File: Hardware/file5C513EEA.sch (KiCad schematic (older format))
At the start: 84 parts, among them J10 IN_2, J11 IN_3, J12 PWM_CV, J13 EXT_CON, J4 OUT2_CON, J5 CUTOFF_CV, J6 SHAPE_CV, J7 SET_CV, J8 OUT1_CON, J9 IN_1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

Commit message: Updated ADSR sliders
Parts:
- removed RV5: ATTACK, Potentiometer_THT:Potentiometer_Bourns_PTA2043_Single_Slide, symbol Device:R_POT_US
- removed RV6: SUSTAIN, Potentiometer_THT:Potentiometer_Bourns_PTA2043_Single_Slide, symbol Device:R_POT_US
- removed RV7: DECAY, Potentiometer_THT:Potentiometer_Bourns_PTA2043_Single_Slide, symbol Device:R_POT_US
- removed RV8: RELEASE, Potentiometer_THT:Potentiometer_Bourns_PTA2043_Single_Slide, symbol Device:R_POT_US
- added RV5: ATTACK, Potentiometer_THT:Potentiometer_Bourns_PTL20_Single_Slide, symbol SID_Parts:BOURNS_PTL
- added RV6: DECAY, Potentiometer_THT:Potentiometer_Bourns_PTL20_Single_Slide, symbol SID_Parts:BOURNS_PTL
- added RV7: SUSTAIN, Potentiometer_THT:Potentiometer_Bourns_PTL20_Single_Slide, symbol SID_Parts:BOURNS_PTL
- added RV8: RELEASE, Potentiometer_THT:Potentiometer_Bourns_PTL20_Single_Slide, symbol SID_Parts:BOURNS_PTL
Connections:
- net 3.3A_IO: now also RV5.1, RV6.1, RV7.1, RV8.1
- net ATTACK_IO: now also RV5.2
- net DECAY_IO: now also RV6.2
- net GND: now also RV5.3, RV6.3, RV7.3, RV8.3
- net RELEASE_IO: now also RV8.2
- net SUSTAIN_IO: now also RV7.2
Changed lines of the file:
@@
 Wire Wire Line
 	1300 4100 1250 4100
-$Comp
-L Device:R_POT_US RV?
-U 1 1 5C5721BD
-P 2200 950
-AR Path="/5BFD63E3/5C5721BD" Ref="RV?"  Part="1"
-AR Path="/5BFD63E3/5C513EEB/5C5721BD" Ref="RV5"  Part="1"
-F 0 "RV5" H 2132 996 50  0000 R CNN
-F 1 "ATTACK" H 2132 905 50  0000 R CNN
-F 2 "Potentiometer_THT:Potentiometer_Bourns_PTA2043_Single_Slide" H 2200 950 50  0001 C CNN
-F 3 "~" H 2200 950 50  0001 C CNN
-	1    2200 950
-	1    0    0    -1
-$EndComp
 Wire Wire Line
 	2200 750  2200 800
@@
 	2450 950  2400 950
 $Comp
-L Device:R_POT_US RV?
-U 1 1 5C5721D4
-P 2300 2050
-AR Path="/5BFD63E3/5C5721D4" Ref="RV?"  Part="1"
-AR Path="/5BFD63E3/5C513EEB/5C5721D4" Ref="RV7"  Part="1"
-F 0 "RV7" H 2232 2096 50  0000 R CNN
-F 1 "DECAY" H 2232 2005 50  0000 R CNN
-F 2 "Potentiometer_THT:Potentiometer_Bourns_PTA2043_Single_Slide" H 2300 2050 50  0001 C CNN
-F 3 "~" H 2300 2050 50  0001 C CNN
-	1    2300 2050
-	1    0    0    -1
-$EndComp
-$Comp
 L power:GND #PWR?
 U 1 1 5C5721E2
@@
 Wire Wire Line
 	2550 2050 2500 2050
-$Comp
-L Device:R_POT_US RV?
-U 1 1 5C5721EB
-P 2200 3150
-AR Path="/5BFD63E3/5C5721EB" Ref="RV?"  Part="1"
-AR Path="/5BFD63E3/5C513EEB/5C5721EB" Ref="RV6"  Part="1"
-F 0 "RV6" H 2132 3196 50  0000 R CNN
-F 1 "SUSTAIN" H 2132 3105 50  0000 R CNN
-F 2 "Potentiometer_THT:Potentiometer_Bourns_PTA2043_Single_Slide" H 2200 3150 50  0001 C CNN
-F 3 "~" H 2200 3150 50  0001 C CNN
-	1    2200 3150
-	1    0    0    -1
-$EndComp
 Wire Wire Line
 	2200 2950 2200 3000
@@
 Wire Wire Line
 	2450 3150 2400 3150
-$Comp
-L Device:R_POT_US RV?
-U 1 1 5C572202
-P 3350 950
-AR Path="/5BFD63E3/5C572202" Ref="RV?"  Part="1"
-AR Path="/5BFD63E3/5C513EEB/5C572202" Ref="RV8"  Part="1"
-F 0 "RV8" H 3282 996 50  0000 R CNN
-F 1 "RELEASE" H 3282 905 50  0000 R CNN
-F 2 "Potentiometer_THT:Potentiometer_Bourns_PTA2043_Single_Slide" H 3350 950 50  0001 C CNN
-F 3 "~" H 3350 950 50  0001 C CNN
-	1    3350 950
-	1    0    0    -1
-$EndComp
 Wire Wire Line
 	3350 750  3350 800
@@
 $Comp
 L Device:C C?
-U 1 1 5C57223C
-P 2400 3350
-AR Path="/5BFD63E3/5C57223C" Ref="C?"  Part="1"
-AR Path="/5BFD63E3/5C513EEB/5C57223C" Ref="C16"  Part="1"
-F 0 "C16" H 2515 3396 50  0000 L CNN
-F 1 "100 nF" H 2515 3305 50  0000 L CNN
-F 2 "Capacitor_SMD:C_0603_1608Metric" H 2438 3200 50  0001 C CNN
-F 3 "~" H 2400 3350 50  0001 C CNN
-	1    2400 3350
-	1    0    0    -1
-$EndComp
-$Comp
-L Device:C C?
 U 1 1 5C572243
 P 3550 1150
@@
 Wire Wire Line
 	2400 3200 2400 3150
-Connection ~ 2400 3150
-Wire Wire Line
-	2400 3150 2350 3150
 Wire Wire Line
 	3550 1000 3550 950
@@
 F 3 "http://ww1.microchip.com/downloads/en/DeviceDoc/21733j.pdf" H 5150 7000 50  0001 C CNN
 	3    5150 7000
-	1    0    0    -1
-$EndComp
-$Comp
-L Device:R_POT_US RV?
-U 1 1 5BF0EB16
-P 3350 2100
-AR Path="/5BFD63E3/5BF0EB16" Ref="RV?"  Part="1"
-AR Path="/5BFD63E3/5C513EEB/5BF0EB16" Ref="RV10"  Part="1"
-F 0 "RV10" H 3282 2146 50  0000 R CNN
-F 1 "SET_ATTEN" H 3282 2055 50  0000 R CNN
-F 2 "Potentiometer_THT:Potentiometer_Bourns_PTV09A-1_Single_Vertical" H 3350 2100 50  0001 C CNN
-F 3 "~" H 3350 2100 50  0001 C CNN
-	1    3350 2100
 	1    0    0    -1
 $EndComp
@@
 Text GLabel 9400 1050 0    50   Input ~ 0
 -10V_REF_IO
+$Comp
+L SID_Parts:BOURNS_PTL RV5
+U 1 1 5BEA495C
+P 2200 700
+F 0 "RV5" H 2112 496 50  0000 R CNN
+F 1 "ATTACK" H 2112 405 50  0000 R CNN
+F 2 "Potentiometer_THT:Potentiometer_Bourns_PTL20_Single_Slide" H 2200 700 50  0001 C CNN
+F 3 "" H 2200 700 50  0001 C CNN
+	1    2200 700
+	1    0    0    -1
+$EndComp
+Connection ~ 2400 3150
+Wire Wire Line
+	2400 3150 2350 3150
+$Comp
+L Device:C C?
+U 1 1 5C57223C
+P 2400 3350
+AR Path="/5BFD63E3/5C57223C" Ref="C?"  Part="1"
+AR Path="/5BFD63E3/5C513EEB/5C57223C" Ref="C16"  Part="1"
+F 0 "C16" H 2515 3396 50  0000 L CNN
+F 1 "100 nF" H 2515 3305 50  0000 L CNN
+F 2 "Capacitor_SMD:C_0603_1608Metric" H 2438 3200 50  0001 C CNN
+F 3 "~" H 2400 3350 50  0001 C CNN
+	1    2400 3350
+	1    0    0    -1
+$EndComp
+$Comp
+L Device:R_POT_US RV?
+U 1 1 5BF0EB16
+P 3350 2100
+AR Path="/5BFD63E3/5BF0EB16" Ref="RV?"  Part="1"
+AR Path="/5BFD63E3/5C513EEB/5BF0EB16" Ref="RV10"  Part="1"
+F 0 "RV10" H 3282 2146 50  0000 R CNN
+F 1 "SET_ATTEN" H 3282 2055 50  0000 R CNN
+F 2 "Potentiometer_THT:Potentiometer_Bourns_PTV09A-1_Single_Vertical" H 3350 2100 50  0001 C CNN
+F 3 "~" H 3350 2100 50  0001 C CNN
+	1    3350 2100
+	1    0    0    -1
+$EndComp
+$Comp
+L SID_Parts:BOURNS_PTL RV8
+U 1 1 5C03E468
+P 3350 700
+F 0 "RV8" H 3262 496 50  0000 R CNN
+F 1 "RELEASE" H 3262 405 50  0000 R CNN
+F 2 "Potentiometer_THT:Potentiometer_Bourns_PTL20_Single_Slide" H 3350 700 50  0001 C CNN
+F 3 "" H 3350 700 50  0001 C CNN
+	1    3350 700
+	1    0    0    -1
+$EndComp
+$Comp
+L SID_Parts:BOURNS_PTL RV6
+U 1 1 5C057FF7
+P 2300 1800
+F 0 "RV6" H 2212 1596 50  0000 R CNN
+F 1 "DECAY" H 2212 1505 50  0000 R CNN
+F 2 "Potentiometer_THT:Potentiometer_Bourns_PTL20_Single_Slide" H 2300 1800 50  0001 C CNN
+F 3 "" H 2300 1800 50  0001 C CNN
+	1    2300 1800
+	1    0    0    -1
+$EndComp
+$Comp
+L SID_Parts:BOURNS_PTL RV7
+U 1 1 5C071B88
+P 2200 2900
+F 0 "RV7" H 2112 2696 50  0000 R CNN
+F 1 "SUSTAIN" H 2112 2605 50  0000 R CNN
+F 2 "Potentiometer_THT:Potentiometer_Bourns_PTL20_Single_Slide" H 2200 2900 50  0001 C CNN
+F 3 "" H 2200 2900 50  0001 C CNN
+	1    2200 2900
+	1    0    0    -1
+$EndComp
 $EndSCHEMATC

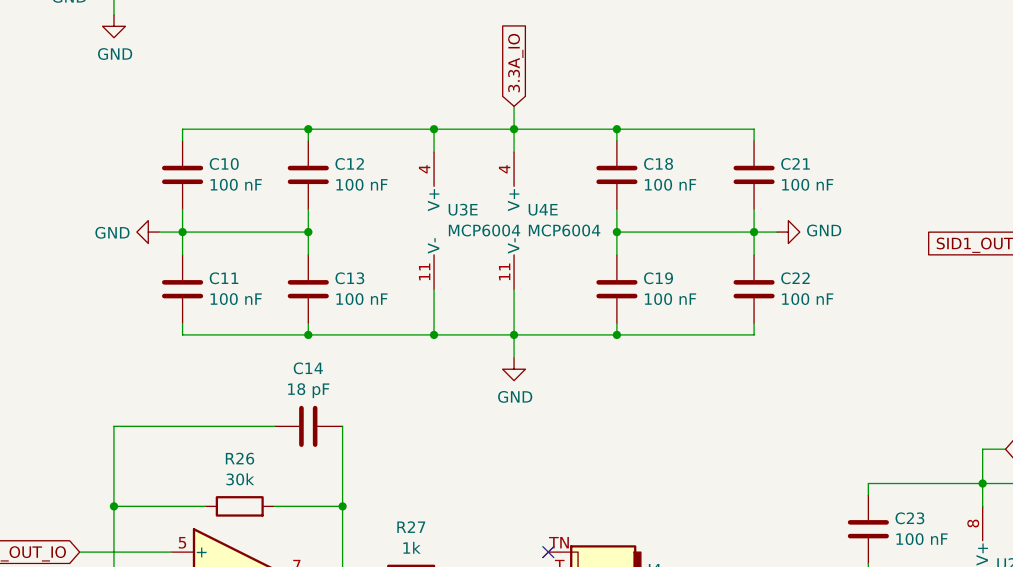
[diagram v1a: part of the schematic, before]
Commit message: More wiring, removed pointless capacitors
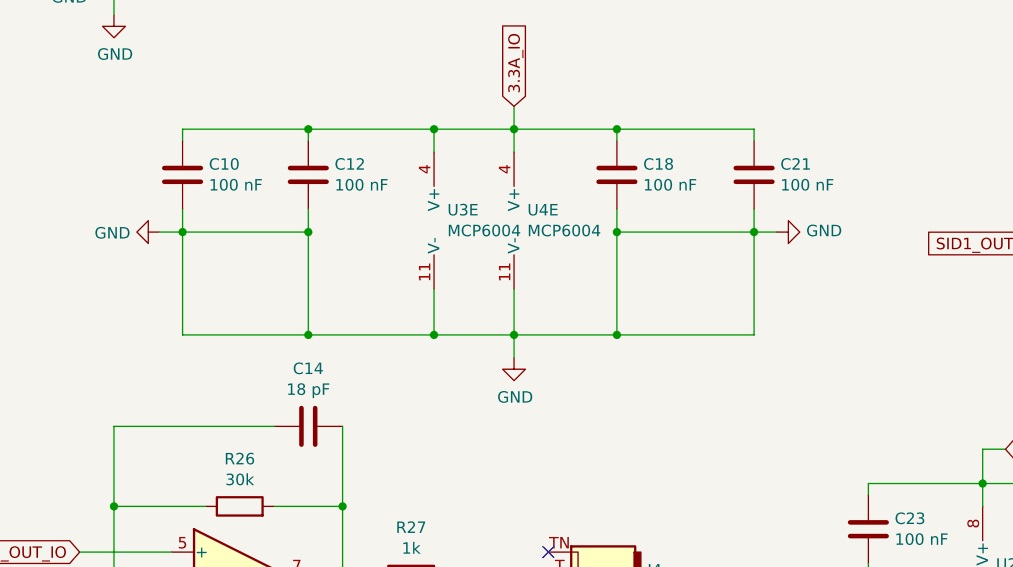
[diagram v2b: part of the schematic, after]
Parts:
- removed C11, C13, C19, C22: 100 nF, Capacitor_SMD:C_0603_1608Metric, symbol Device:C
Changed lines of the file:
@@
 	1    0    0    -1
 $EndComp
-$Comp
-L Device:C C?
-U 1 1 5C593892
-P 1550 5750
-AR Path="/5BFD63E3/5C593892" Ref="C?"  Part="1"
-AR Path="/5BFD63E3/5C513EEB/5C593892" Ref="C11"  Part="1"
-F 0 "C11" H 1665 5796 50  0000 L CNN
-F 1 "100 nF" H 1665 5705 50  0000 L CNN
-F 2 "Capacitor_SMD:C_0603_1608Metric" H 1588 5600 50  0001 C CNN
-F 3 "~" H 1550 5750 50  0001 C CNN
-	1    1550 5750
-	1    0    0    -1
-$EndComp
-$Comp
-L Device:C C?
-U 1 1 5C593899
-P 3450 5750
-AR Path="/5BFD63E3/5C593899" Ref="C?"  Part="1"
-AR Path="/5BFD63E3/5C513EEB/5C593899" Ref="C19"  Part="1"
-F 0 "C19" H 3565 5796 50  0000 L CNN
-F 1 "100 nF" H 3565 5705 50  0000 L CNN
-F 2 "Capacitor_SMD:C_0603_1608Metric" H 3488 5600 50  0001 C CNN
-F 3 "~" H 3450 5750 50  0001 C CNN
-	1    3450 5750
-	1    0    0    -1
-$EndComp
-Wire Wire Line
-	1550 5900 1550 5950
 Connection ~ 3000 5950
-Wire Wire Line
-	3450 5950 3450 5900
 Wire Wire Line
 	1550 5100 1550 5050
@@
 Wire Wire Line
 	1550 5500 1550 5400
-Wire Wire Line
-	1550 5600 1550 5500
 Connection ~ 1550 5500
 $Comp
@@
 	1    0    0    -1
 $EndComp
-$Comp
-L Device:C C?
-U 1 1 5C16FA07
-P 4050 5750
-AR Path="/5BFD63E3/5C16FA07" Ref="C?"  Part="1"
-AR Path="/5BFD63E3/5C513EEB/5C16FA07" Ref="C22"  Part="1"
-F 0 "C22" H 4165 5796 50  0000 L CNN
-F 1 "100 nF" H 4165 5705 50  0000 L CNN
-F 2 "Capacitor_SMD:C_0603_1608Metric" H 4088 5600 50  0001 C CNN
-F 3 "~" H 4050 5750 50  0001 C CNN
-	1    4050 5750
-	1    0    0    -1
-$EndComp
 Wire Wire Line
 	3450 5050 4050 5050
@@
 Wire Wire Line
 	3450 5950 4050 5950
-Wire Wire Line
-	4050 5950 4050 5900
 Connection ~ 3450 5950
 Wire Wire Line
@@
 	4150 5500 4050 5500
 Connection ~ 4050 5500
-Wire Wire Line
-	4050 5500 4050 5600
 $Comp
 L Device:C C?
@@
 	1    0    0    -1
 $EndComp
-$Comp
-L Device:C C?
-U 1 1 5C1D88B3
-P 2100 5750
-AR Path="/5BFD63E3/5C1D88B3" Ref="C?"  Part="1"
-AR Path="/5BFD63E3/5C513EEB/5C1D88B3" Ref="C13"  Part="1"
-F 0 "C13" H 2215 5796 50  0000 L CNN
-F 1 "100 nF" H 2215 5705 50  0000 L CNN
-F 2 "Capacitor_SMD:C_0603_1608Metric" H 2138 5600 50  0001 C CNN
-F 3 "~" H 2100 5750 50  0001 C CNN
-	1    2100 5750
-	1    0    0    -1
-$EndComp
 Wire Wire Line
 	1550 5050 2100 5050
@@
 Wire Wire Line
 	1550 5500 2100 5500
-Connection ~ 2100 5500
-Wire Wire Line
-	2100 5500 2100 5600
-Wire Wire Line
-	2100 5950 2100 5900
 Wire Wire Line
 	1550 5950 2100 5950
@@
 	2650 5750 2650 5950
 Connection ~ 3450 5500
-Wire Wire Line
-	3450 5500 3450 5600
 $Comp
 L Device:D_Zener D?
@@
 	1    0    0    -1
 $EndComp
+Wire Wire Line
+	1550 5500 1550 5950
+Wire Wire Line
+	2100 5500 2100 5950
+Connection ~ 2100 5500
+Wire Wire Line
+	3450 5500 3450 5950
+Wire Wire Line
+	4050 5500 4050 5950
 $EndSCHEMATC

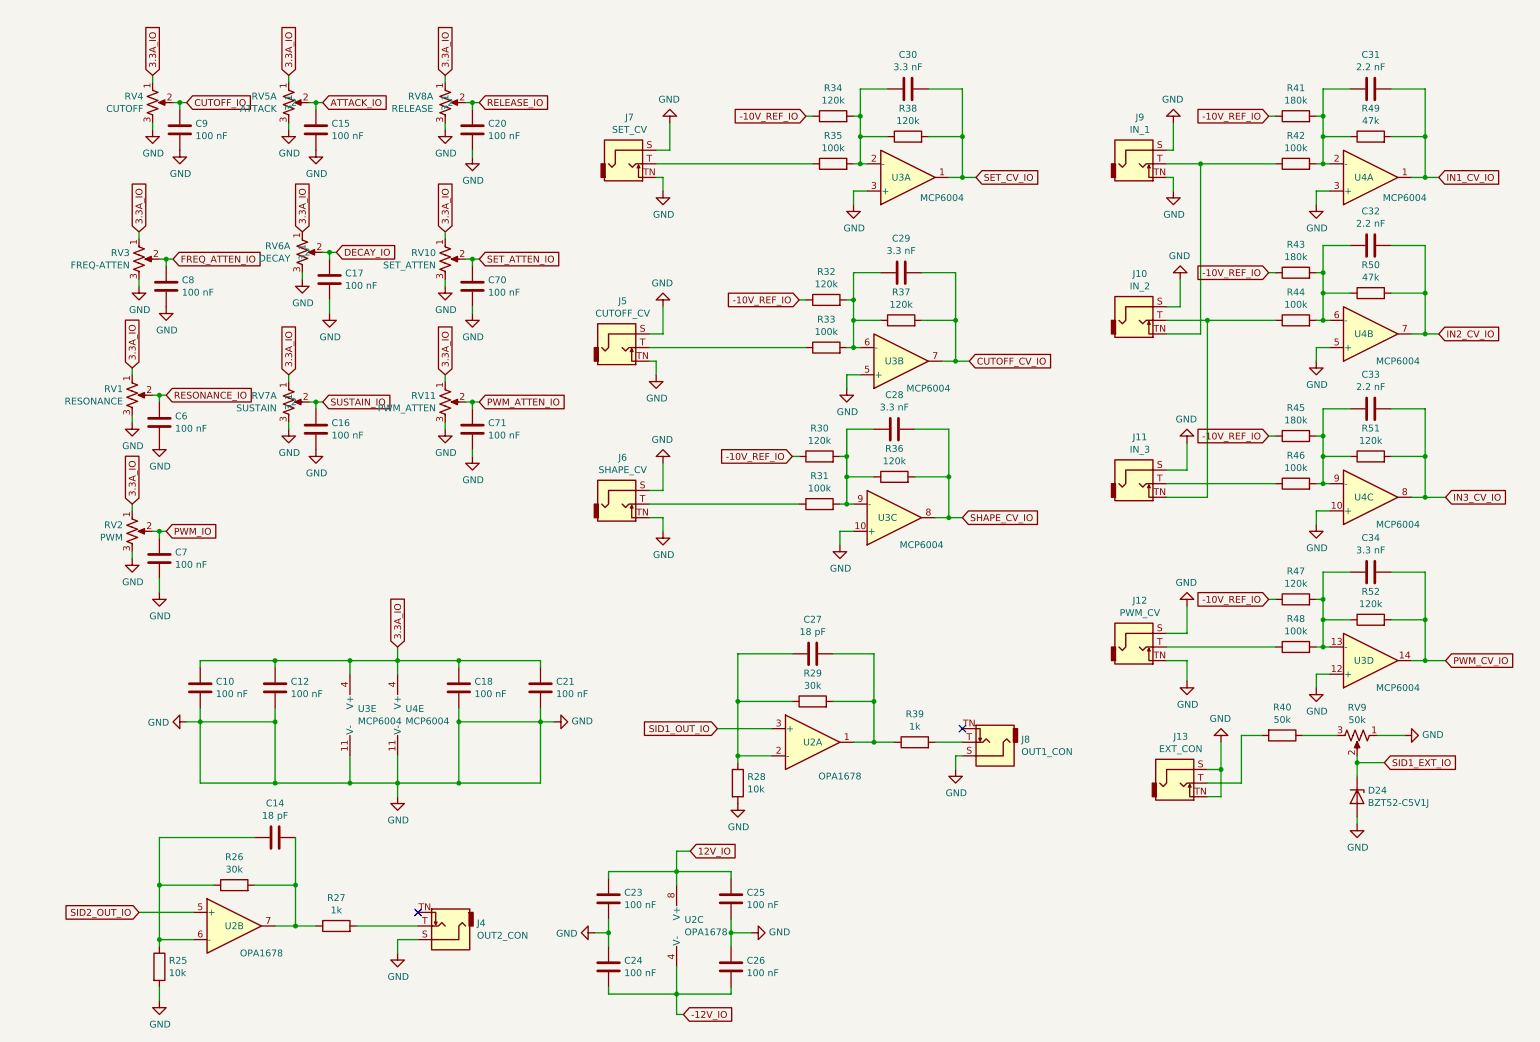
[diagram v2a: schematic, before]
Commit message: Updated to single four layer board
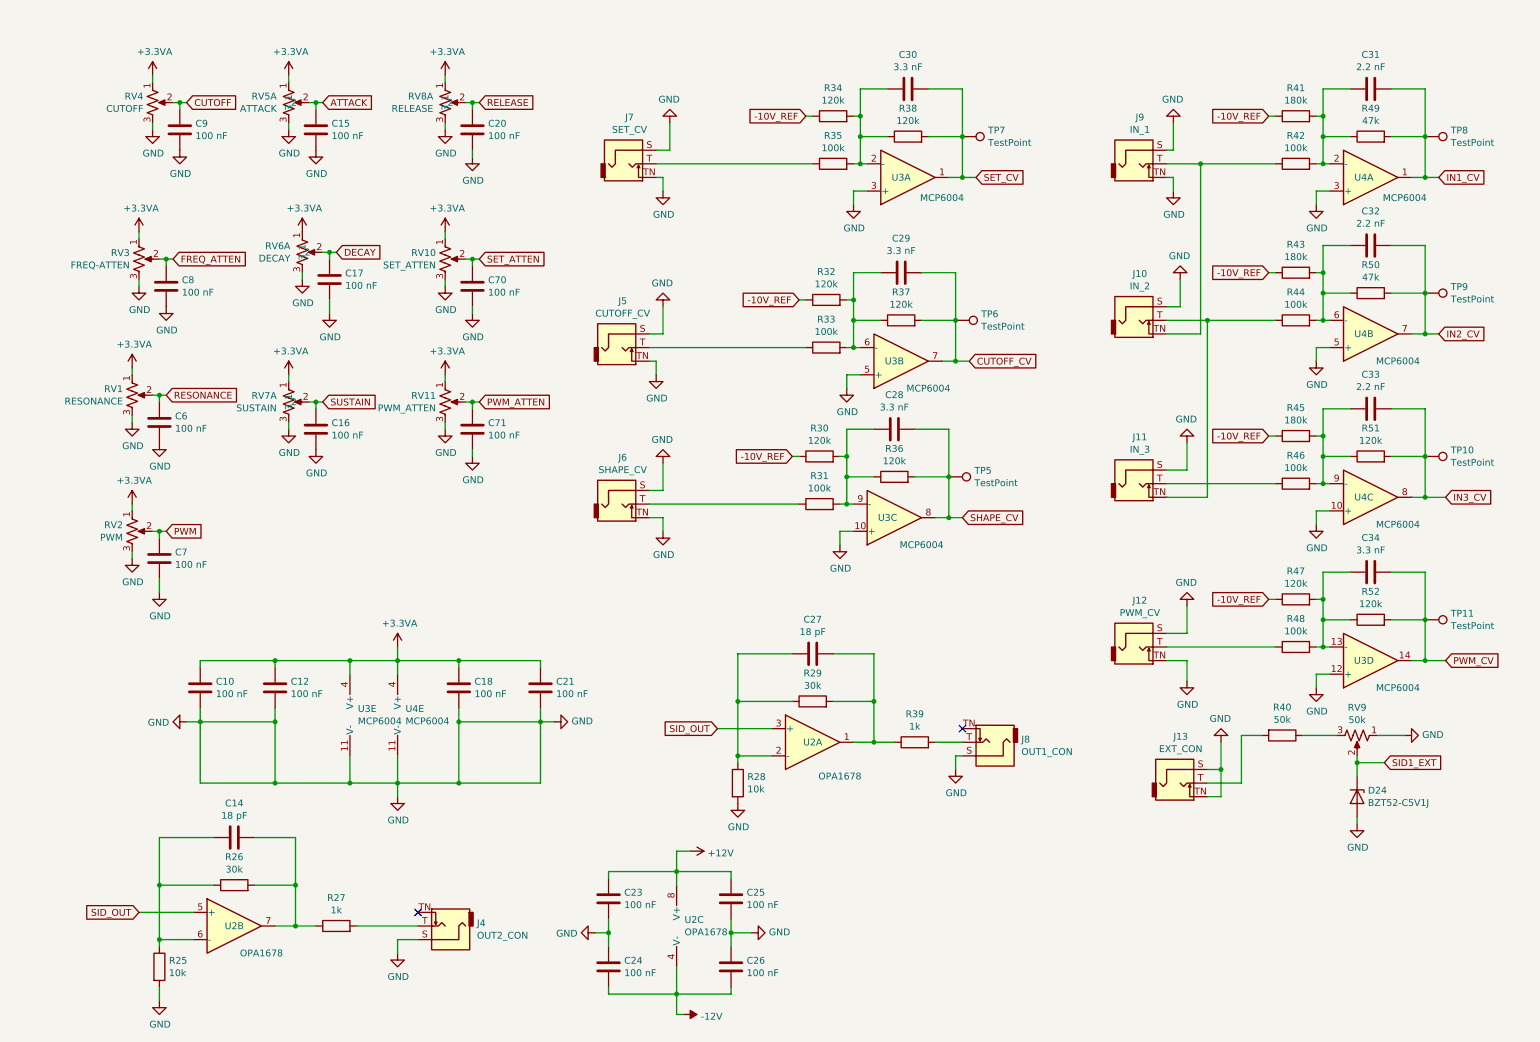
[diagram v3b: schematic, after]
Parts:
- added TP10, TP11, TP5, TP6, TP7, TP8, TP9: TestPoint, TestPoint:TestPoint_Pad_D1.0mm, symbol Connector:TestPoint
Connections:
- net SID2_OUT_IO is gone; now on net SID_OUT: U2.5 (+)
- net -10V_REF_IO renamed -10V_REF
- net -12V_IO renamed -12V
- net 12V_IO renamed +12V
- net 3.3A_IO renamed +3.3VA
- net ATTACK_IO renamed ATTACK
- net CUTOFF_CV_IO renamed CUTOFF_CV
- net CUTOFF_CV: now also TP6.1
- net CUTOFF_IO renamed CUTOFF
- net DECAY_IO renamed DECAY
- net FREQ_ATTEN_IO renamed FREQ_ATTEN
- net IN1_CV_IO renamed IN1_CV
- net IN1_CV: now also TP8.1
- net IN2_CV_IO renamed IN2_CV
- net IN2_CV: now also TP9.1
- net IN3_CV_IO renamed IN3_CV
- net IN3_CV: now also TP10.1
- net PWM_ATTEN_IO renamed PWM_ATTEN
- net PWM_CV_IO renamed PWM_CV
- net PWM_CV: now also TP11.1
- net PWM_IO renamed PWM
- net RELEASE_IO renamed RELEASE
- net RESONANCE_IO renamed RESONANCE
- net SET_ATTEN_IO renamed SET_ATTEN
- net SET_CV_IO renamed SET_CV
- net SET_CV: now also TP7.1
- net SHAPE_CV_IO renamed SHAPE_CV
- net SHAPE_CV: now also TP5.1
- net SID1_EXT_IO renamed SID1_EXT
- net SID1_OUT_IO renamed SID_OUT
- net SUSTAIN_IO renamed SUSTAIN
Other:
- moved on the sheet: C14
